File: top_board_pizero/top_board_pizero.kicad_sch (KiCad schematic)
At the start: 43 parts, among them J3 Pi Zero 2, J4 FFC_1, J5 FFC_2, J6 SH 4P, J7 SH 4P, J8 SH 4P, J9 SH 4P, U21 TPAZ1043-04F, U27 XL9535QF24, U28 XL9535QF24, U29 PI3USB42ZMEX, U30 PI3USB42ZMEX, U32 BL24C32A, U33 BL24C32A, U4 ESP32-C6-WROOM-1, U6 PI3USB42ZMEX

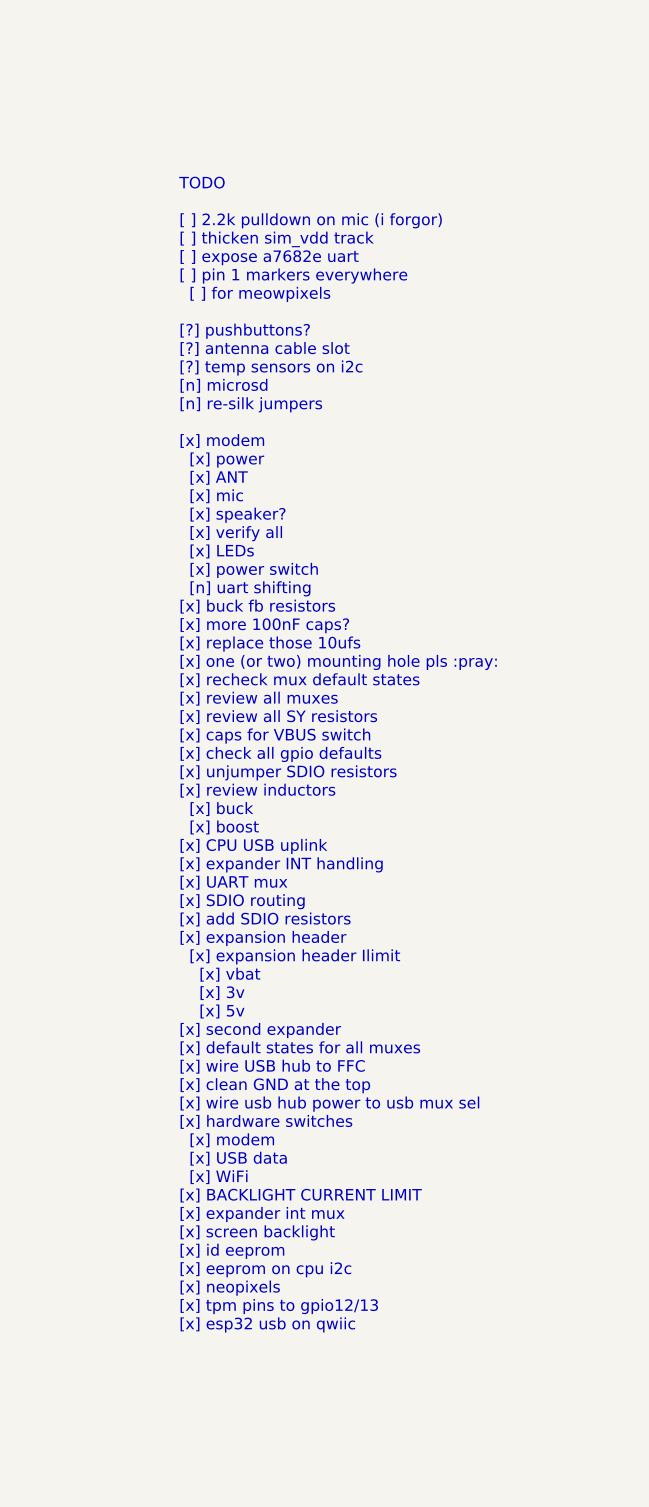
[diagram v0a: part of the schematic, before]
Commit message: small tweaks post-ordering (todo entries and step export settings)
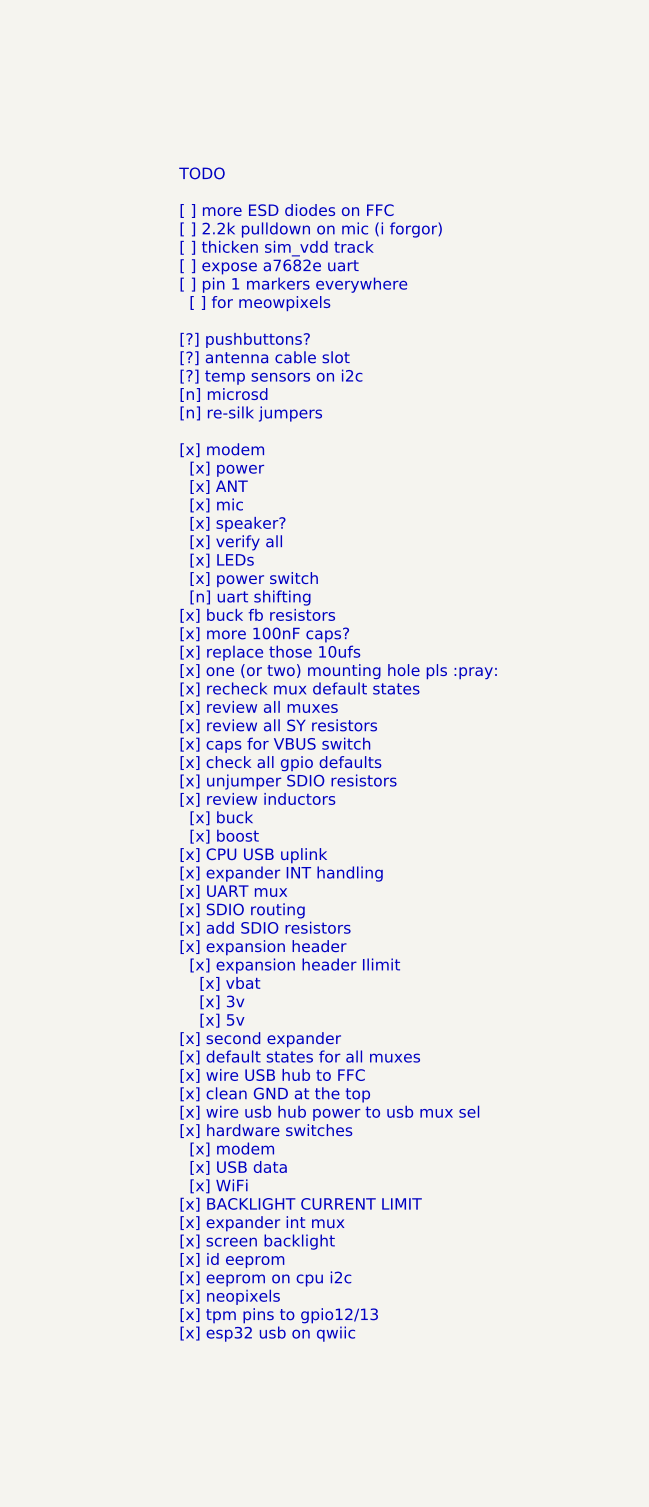
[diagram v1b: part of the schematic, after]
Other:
- note added: "TODO [ ] more ESD diodes on FFC [ ] 2.2k pulldown on mic (i forgor) [ ] thicken sim_vdd track [ ] expose a7682e uart [ ] pin 1 markers everywhere [ ] for meowpixels [?] pushbuttons? [?] antenna cable slot [?] temp sensors on i2c [n] microsd [n] re-silk jumpers [x] modem [x] power [x] ANT [x] mic [x] speaker? [x] verify all [x] LEDs [x] power switch [n] uart shifting [x] buck fb resistors [x] more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"
- note removed: "TODO [ ] 2.2k pulldown on mic (i forgor) [ ] thicken sim_vdd track [ ] expose a7682e uart [ ] pin 1 markers everywhere [ ] for meowpixels [?] pushbuttons? [?] antenna cable slot [?] temp sensors on i2c [n] microsd [n] re-silk jumpers [x] modem [x] power [x] ANT [x] mic [x] speaker? [x] verify all [x] LEDs [x] power switch [n] uart shifting [x] buck fb resistors [x] more 100nF caps? [x] replace th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"
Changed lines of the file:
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@@
 		)
 	)
-	(text "TODO\n\n[ ] 2.2k pulldown on mic (i forgor)\n[ ] thicken sim_vdd track\n[ ] expose a7682e uart\n[ ] pin 1 markers everywhere\n  [ ] for meowpixels\n\n[?] pushbuttons?\n[?] antenna cable slot\n[?] temp sensors on i2c\n[n] microsd\n[n] re-silk jumpers\n\n[x] modem\n  [x] power\n  [x] ANT\n  [x] mic\n  [x] speaker?\n  [x] verify all\n  [x] LEDs\n  [x] power switch\n  [n] uart shifting\n[x] buck fb resistors\n[x] more 100nF caps?\n[x] replace those 10ufs\n[x] one (or two) mounting hole pls :pray:\n[x] recheck mux default states\n[x] review all muxes\n[x] review all SY resistors\n[x] caps for VBUS switch\n[x] check all gpio defaults\n[x] unjumper SDIO resistors\n[x] review inductors\n  [x] buck\n  [x] boost\n[x] CPU USB uplink\n[x] expander INT handling\n[x] UART mux\n[x] SDIO routing\n[x] add SDIO resistors\n[x] expansion header\n  [x] expansion header Ilimit\n    [x] vbat\n    [x] 3v\n    [x] 5v\n[x] second expander\n[x] default states for all muxes\n[x] wire USB hub to FFC\n[x] clean GND at the top\n[x] wire usb hub power to usb mux sel\n[x] hardware switches\n  [x] modem\n  [x] USB data\n  [x] WiFi\n[x] BACKLIGHT CURRENT LIMIT\n[x] expander int mux\n[x] screen backlight\n[x] id eeprom\n[x] eeprom on cpu i2c\n[x] neopixels\n[x] tpm pins to gpio12/13\n[x] esp32 usb on qwiic"
+	(text "TODO\n\n[ ] more ESD diodes on FFC\n[ ] 2.2k pulldown on mic (i forgor)\n[ ] thicken sim_vdd track\n[ ] expose a7682e uart\n[ ] pin 1 markers everywhere\n  [ ] for meowpixels\n\n[?] pushbuttons?\n[?] antenna cable slot\n[?] temp sensors on i2c\n[n] microsd\n[n] re-silk jumpers\n\n[x] modem\n  [x] power\n  [x] ANT\n  [x] mic\n  [x] speaker?\n  [x] verify all\n  [x] LEDs\n  [x] power switch\n  [n] uart shifting\n[x] buck fb resistors\n[x] more 100nF caps?\n[x] replace those 10ufs\n[x] one (or two) mounting hole pls :pray:\n[x] recheck mux default states\n[x] review all muxes\n[x] review all SY resistors\n[x] caps for VBUS switch\n[x] check all gpio defaults\n[x] unjumper SDIO resistors\n[x] review inductors\n  [x] buck\n  [x] boost\n[x] CPU USB uplink\n[x] expander INT handling\n[x] UART mux\n[x] SDIO routing\n[x] add SDIO resistors\n[x] expansion header\n  [x] expansion header Ilimit\n    [x] vbat\n    [x] 3v\n    [x] 5v\n[x] second expander\n[x] default states for all muxes\n[x] wire USB hub to FFC\n[x] clean GND at the top\n[x] wire usb hub power to usb mux sel\n[x] hardware switches\n  [x] modem\n  [x] USB data\n  [x] WiFi\n[x] BACKLIGHT CURRENT LIMIT\n[x] expander int mux\n[x] screen backlight\n[x] id eeprom\n[x] eeprom on cpu i2c\n[x] neopixels\n[x] tpm pins to gpio12/13\n[x] esp32 usb on qwiic"
 		(exclude_from_sim no)
 		(at 304.8 100.838 0)
